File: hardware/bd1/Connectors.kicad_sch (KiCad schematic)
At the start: 7 parts, among them J2 USB_C_Receptacle_USB2.0, J20 USB_C_Receptacle_USB2.0, J3 SJ-43514, J30 SJ-43514, U2 AP2127N-3.3

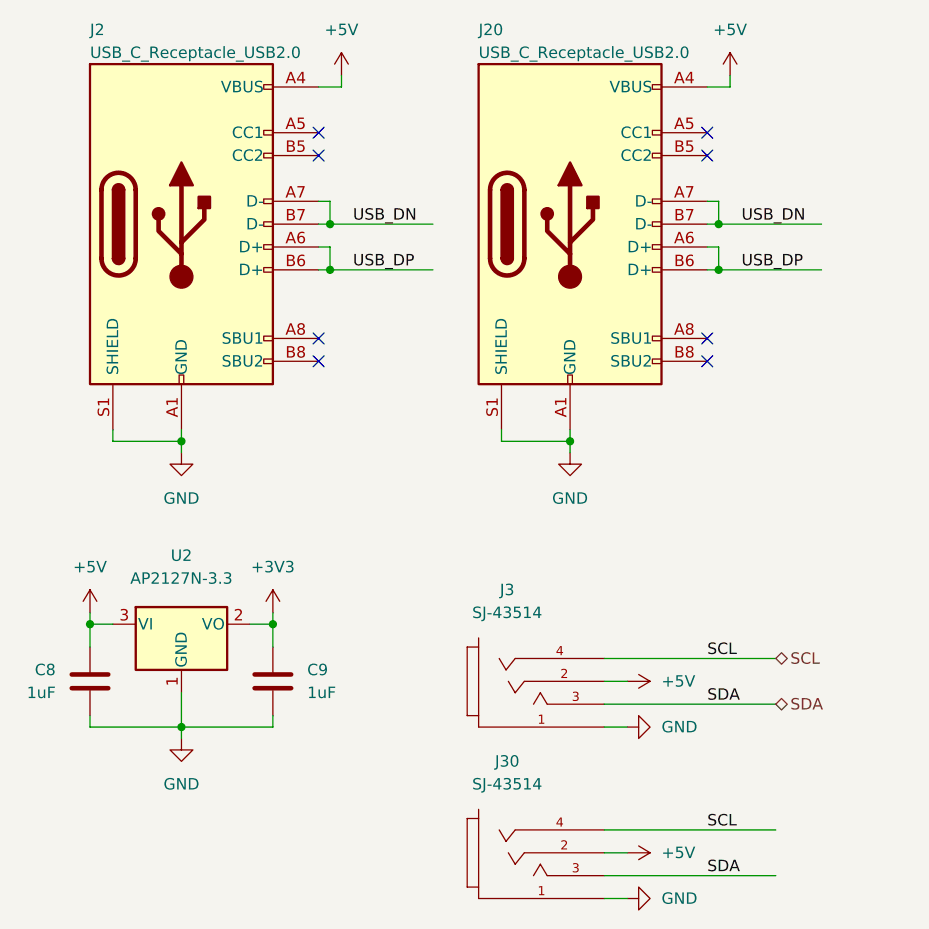
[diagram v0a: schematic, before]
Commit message: USB routing
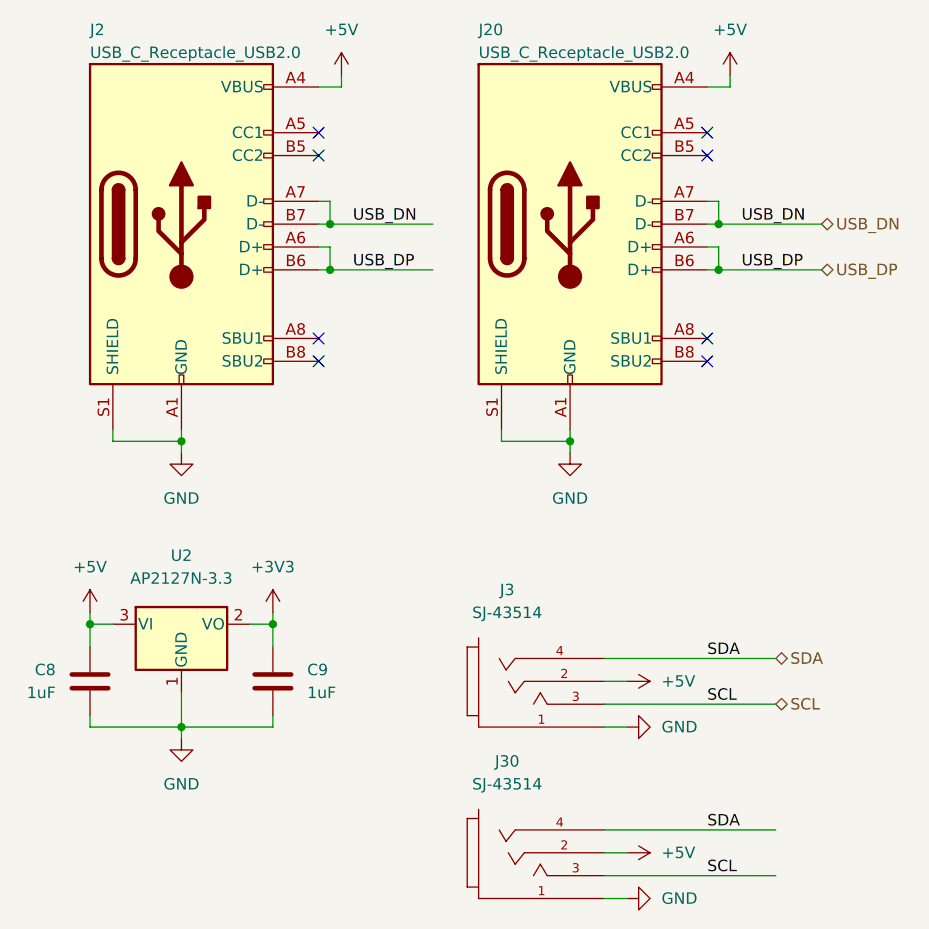
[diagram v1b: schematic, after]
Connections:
- net SCL: now also J3.3 (Ring1), J30.3 (Ring1); no longer J3.4 (Ring2), J30.4 (Ring2)
- net SDA: now also J3.4 (Ring2), J30.4 (Ring2); no longer J3.3 (Ring1), J30.3 (Ring1)
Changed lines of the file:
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@@
 		)
 	)
-	(label "SCL"
+	(label "SDA"
+		(at 185.42 115.57 0)
+		(fields_autoplaced yes)
+		(effects
+			(font
+				(size 1.27 1.27)
+			)
+			(justify left bottom)
+		)
+	)
+	(label "SDA"
 		(at 185.42 134.62 0)
 		(fields_autoplaced yes)
@@
 		)
 	)
-	(label "SDA"
+	(label "SCL"
 		(at 185.42 120.65 0)
+		(fields_autoplaced yes)
+		(effects
+			(font
+				(size 1.27 1.27)
+			)
+			(justify left bottom)
+		)
+	)
+	(label "SCL"
+		(at 185.42 139.7 0)
 		(fields_autoplaced yes)
 		(effects
@@
 	(label "USB_DN"
 		(at 146.05 67.31 0)
-		(fields_autoplaced yes)
-		(effects
-			(font
-				(size 1.27 1.27)
-			)
-			(justify left bottom)
-		)
-	)
-	(label "SDA"
-		(at 185.42 139.7 0)
 		(fields_autoplaced yes)
 		(effects
@@
 		)
 	)
-	(label "SCL"
-		(at 185.42 115.57 0)
-		(fields_autoplaced yes)
-		(effects
-			(font
-				(size 1.27 1.27)
-			)
-			(justify left bottom)
-		)
-	)
 	(label "USB_DN"
 		(at 189.23 67.31 0)
@@
 		)
 	)
-	(hierarchical_label "SCL"
+	(hierarchical_label "USB_DP"
+		(shape bidirectional)
+		(at 198.12 72.39 0)
+		(fields_autoplaced yes)
+		(effects
+			(font
+				(size 1.27 1.27)
+			)
+			(justify left)
+		)
+	)
+	(hierarchical_label "SDA"
 		(shape bidirectional)
 		(at 193.04 115.57 0)
@@
 		)
 	)
-	(hierarchical_label "SDA"
+	(hierarchical_label "SCL"
 		(shape bidirectional)
 		(at 193.04 120.65 0)
 		(fields_autoplaced yes)
 		(effects
+			(font
+				(size 1.27 1.27)
+			)
+			(justify left)
+		)
+	)
+	(hierarchical_label "USB_DN"
+		(shape bidirectional)
+		(at 198.12 67.31 0)
+		(fields_autoplaced yes)
+		(effects
